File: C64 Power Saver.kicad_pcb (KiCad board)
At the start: 2 copper layers, 65.4 x 39.4 mm, 17 parts, among them J1 5V_INPUT, J2 5V_OUTPUT, J3 9VAC_INPUT, J4 9VAC_OUTPUT, K1 SANYOU_SRD_Form_C, Q1 PN2222A, Q2 PN2222A

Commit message: Oh... So I made a saver that works only on bad ones... Rev. B!
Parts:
- D1: value 4.7v -> 1N4732A
- D2: value 1N914 -> 1N4148
- D4: value OV -> BAD
- Q1, Q2: footprint TO_SOT_Packages_THT:TO-92_Molded_Narrow -> TO_SOT_Packages_THT:TO-92_Inline_Wide
- moved D4 8.71 mm to (125.2, 94.2)
- moved D3 7.83 mm to (125.2, 102.4)
- moved R4 3.81 mm to (109.2, 104.1)
- moved R5 3.81 mm to (109.2, 100.3)
- moved Q1 2.54 mm to (105.4, 102.9)
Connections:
- K1 pad 3: Net-(K1-Pad3) -> 5V_OUT
- K1 pad 4: 5V_OUT -> Net-(K1-Pad4)
- R5 pad 1: Net-(K1-Pad3) -> Net-(K1-Pad4)
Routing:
- net Net-(K1-Pad4): track 0.00 -> 21.9 mm
- net Net-(K1-Pad3): track 15.5 -> 0.00 mm
- net Net-(D3-Pad2): track 9.42 -> 4.04 mm
- net Net-(D1-Pad2): track 12.7 -> 15.8 mm
- net 5V_OUT: track 31.6 -> 28.6 mm
- net Net-(D4-Pad2): track 4.97 -> 7.46 mm
- net Net-(Q1-Pad3): track 31.2 -> 33.0 mm
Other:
- board text added: "C64 Power Saver Revision B https://hvetebolle.blogspot.com/"
- board text removed: "C64 Power Saver Revision A https://hvetebolle.blogspot.com/"

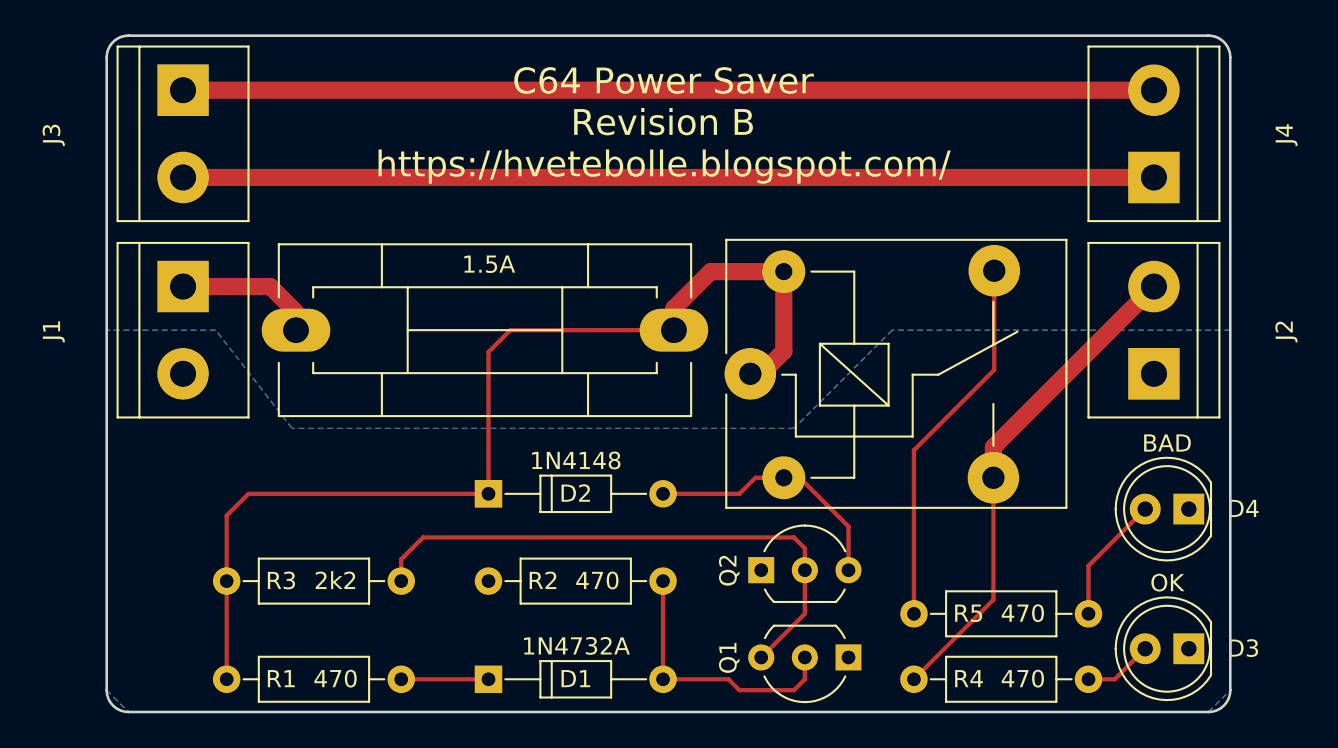
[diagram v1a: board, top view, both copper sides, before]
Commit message: PCB layout redone with DIN connector and added 5v buzzer
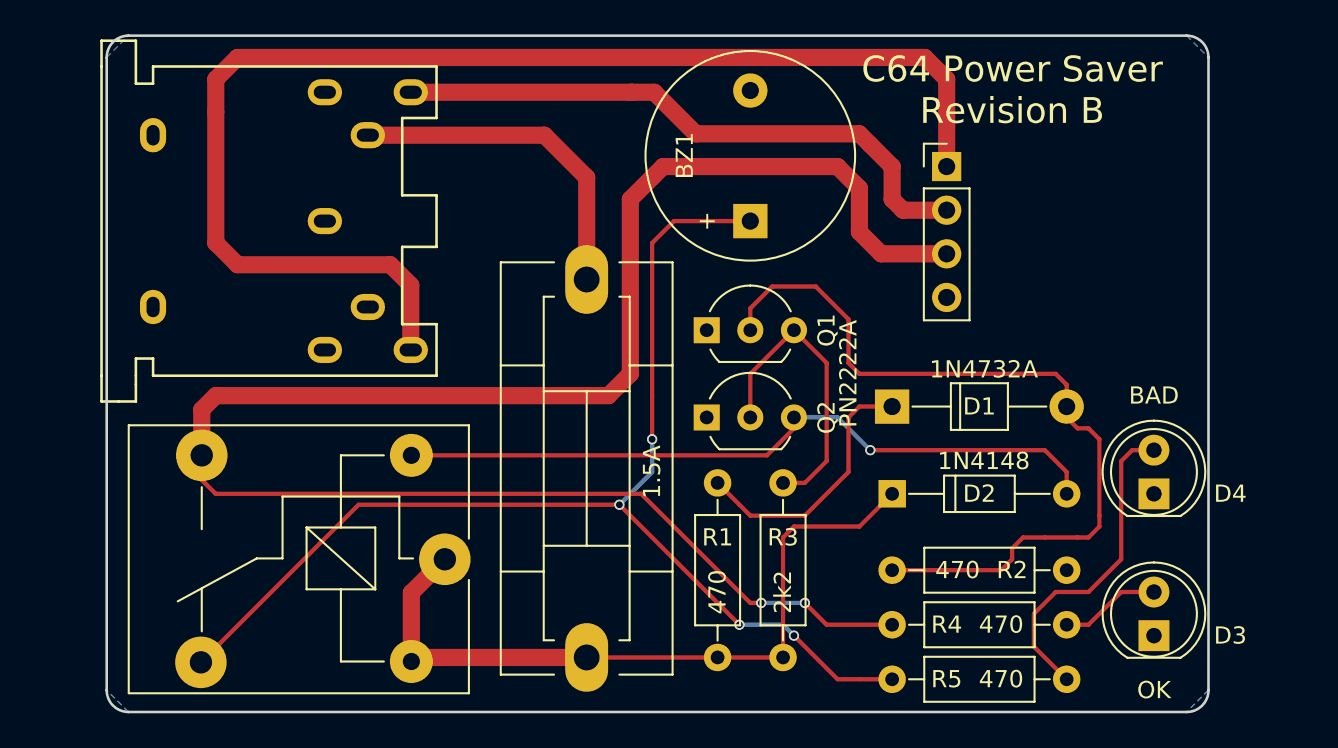
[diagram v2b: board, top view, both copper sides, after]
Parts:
- removed J2: 5V_OUTPUT, Connectors_Terminal_Blocks:TerminalBlock_bornier-2_P5.08mm
- removed J3: 9VAC_INPUT, Connectors_Terminal_Blocks:TerminalBlock_bornier-2_P5.08mm
- removed J4: 9VAC_OUTPUT, Connectors_Terminal_Blocks:TerminalBlock_bornier-2_P5.08mm
- added BZ1: Buzzer, Buzzers_Beepers:Buzzer_12x9.5RM7.6, F.Cu at (99.7, 77.5)
- added J5: DIN-7, C64_PWR:C64_PWR, F.Cu at (74.9, 77.5)
- D1: footprint Diodes_THT:D_DO-35_SOD27_P10.16mm_Horizontal -> Diodes_THT:D_T-1_P10.16mm_Horizontal
- J1: value 5V_INPUT -> OUTPUT; footprint Connectors_Terminal_Blocks:TerminalBlock_bornier-2_P5.08mm -> C64_PWR:OUTPUT_ZIP
- moved J1 45.0 mm to (111.1, 74.3), turned to 0 degrees
- moved R3 32.7 mm to (101.6, 102.9), turned to 90 degrees
- moved R1 28.6 mm to (97.8, 102.9), turned to 90 degrees
- moved D1 28.4 mm to (108.0, 88.3)
- moved D2 23.5 mm to (108.0, 93.3)
- moved K1 20.8 mm to (81.9, 97.2), turned to 180 degrees
- moved Q1 20.8 mm to (97.2, 83.8), turned to 0 degrees
- moved F1 19.7 mm to (90.2, 102.9), turned to 90 degrees
- moved R2 13.4 mm to (108.0, 97.8), turned to 0 degrees
- moved Q2 9.44 mm to (97.2, 88.9)
- moved R5 4.02 mm to (108.0, 104.1)
- moved R4 3.42 mm to (108.0, 101.0)
- moved D4 2.22 mm to (123.2, 93.3), turned to 90 degrees
- moved D3 2.17 mm to (123.2, 101.6), turned to 90 degrees
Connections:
- J1 pad 1: 5V_IN -> 9VAC_2
- J1 pad 2: GND -> 9VAC_1
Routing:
- net 5V_OUT: track 28.6 -> 106.5 mm, vias 0 -> 2
- net Net-(BZ1-Pad1): track 21.9 -> 70.5 mm, vias 0 -> 4
- net Net-(D1-Pad2): track 15.8 -> 47.0 mm
- net Net-(D2-Pad2): track 14.9 -> 42.0 mm, vias 0 -> 1
- net 9VAC_1: track 56.5 -> 35.2 mm
- net 9VAC_2: track 56.5 -> 74.5 mm
- net Net-(D2-Pad1): track 60.5 -> 42.9 mm
- net Net-(Q1-Pad3): track 33.0 -> 17.6 mm
- net 5V_IN: track 8.24 -> 19.7 mm
- net Net-(D4-Pad2): track 7.46 -> 18.9 mm
- net Net-(D1-Pad1): track 5.08 -> 15.4 mm
- net Net-(D3-Pad2): track 4.04 -> 5.87 mm
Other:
- board size 65.4 x 39.4 mm -> 64.1 x 39.4 mm
- board text added: "C64 Power Saver Revision B"
- board text added: "https://hvetebolle.blogspot.com/"
- board text removed: "5V INPUT"
- board text removed: "5V OUTPUT"
- board text removed: "9V AC"
- board text removed: "C64 Power Saver Revision B https://hvetebolle.blogspot.com/"
- board text removed: "GND"

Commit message: Fixed groundplane and made wire solder points larger
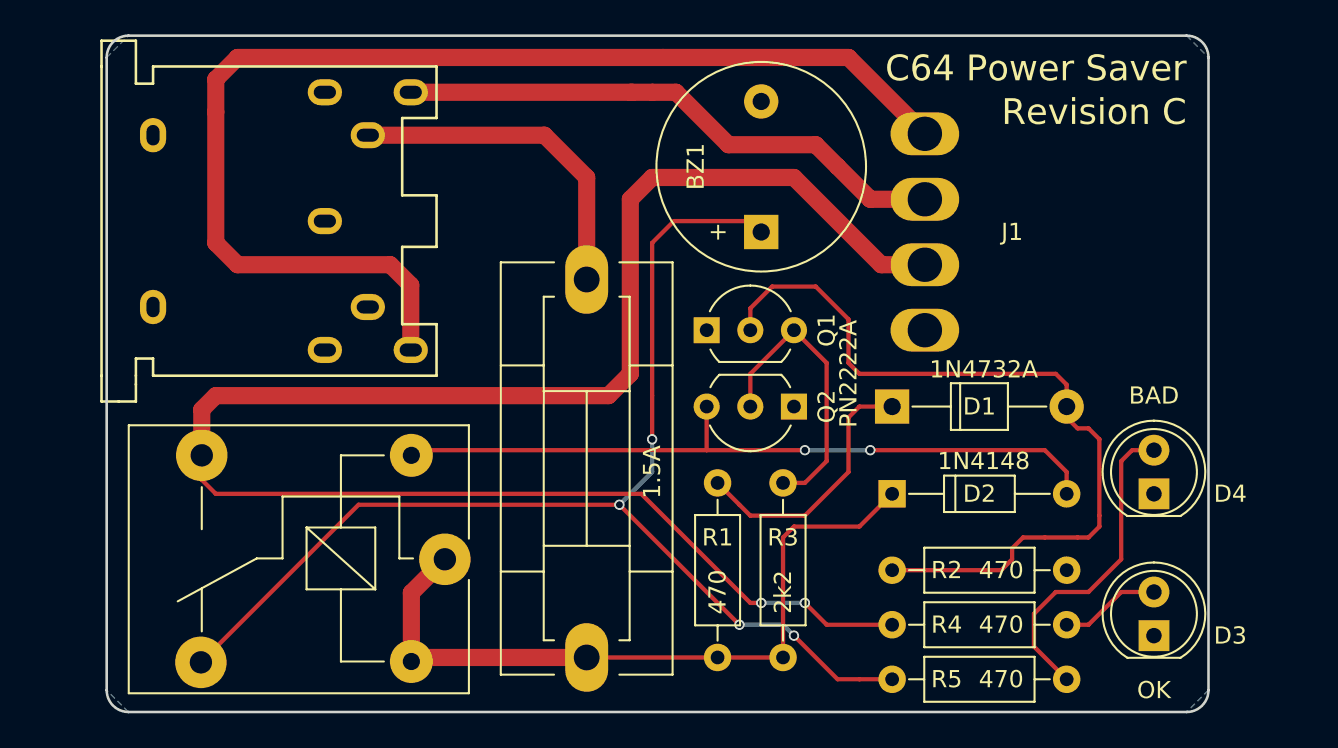
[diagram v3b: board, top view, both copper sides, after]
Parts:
- moved Q2 5.12 mm to (102.2, 88.3), turned to 180 degrees
- moved BZ1 0.90 mm to (100.3, 78.1)
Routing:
- net 9VAC_2: track 74.5 -> 69.4 mm
- net 5V_OUT: track 106.5 -> 103.5 mm
- net 9VAC_1: track 35.2 -> 32.5 mm
- net Net-(Q1-Pad3): track 17.6 -> 17.0 mm
- net Net-(D2-Pad2): track 42.0 -> 42.6 mm, vias 1 -> 2
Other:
- board text added: "C64 Power Saver"
- board text added: "Revision C"
- board text removed: "C64 Power Saver Revision B"

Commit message: Added wire pads for +5v and GND for thicker wires when internal mounting
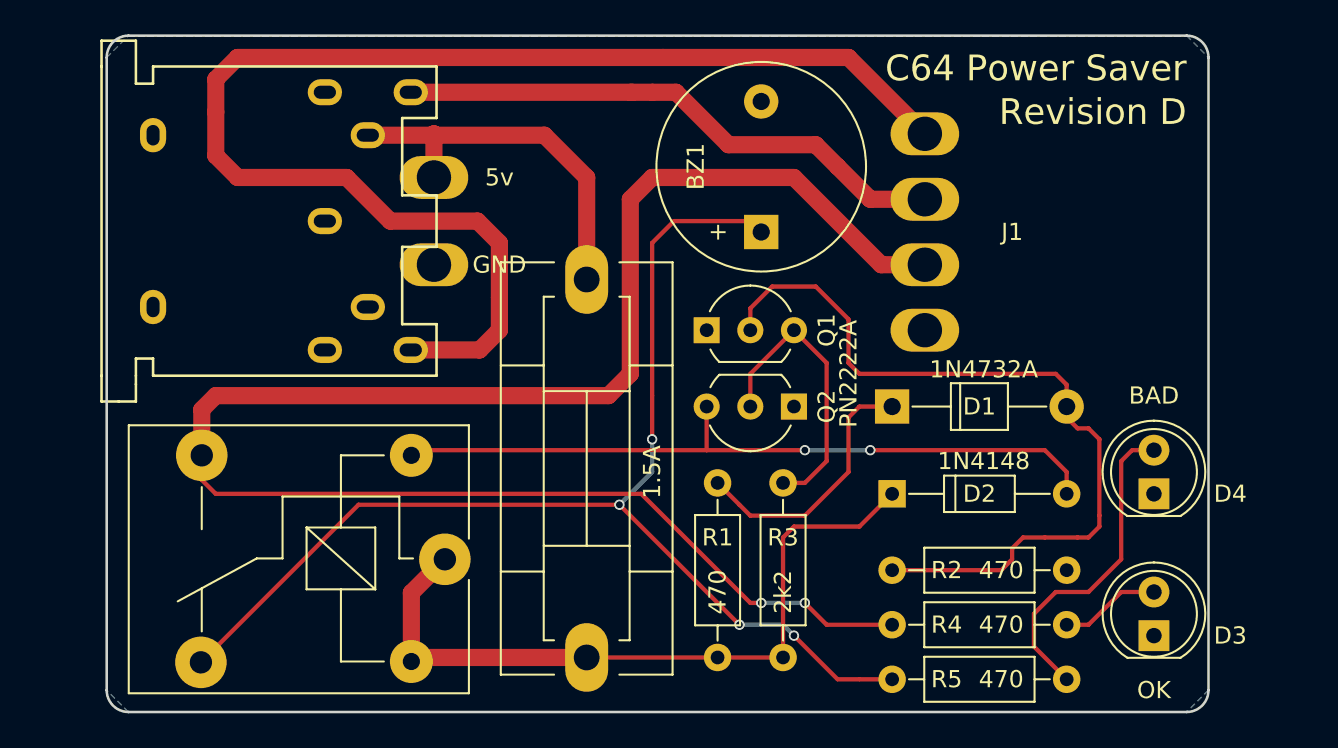
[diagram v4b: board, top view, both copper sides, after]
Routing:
- net 9VAC_2: track 69.4 -> 77.4 mm
- net 5V_IN: track 19.7 -> 22.3 mm
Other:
- board text added: "Revision D"
- board text removed: "Revision C"

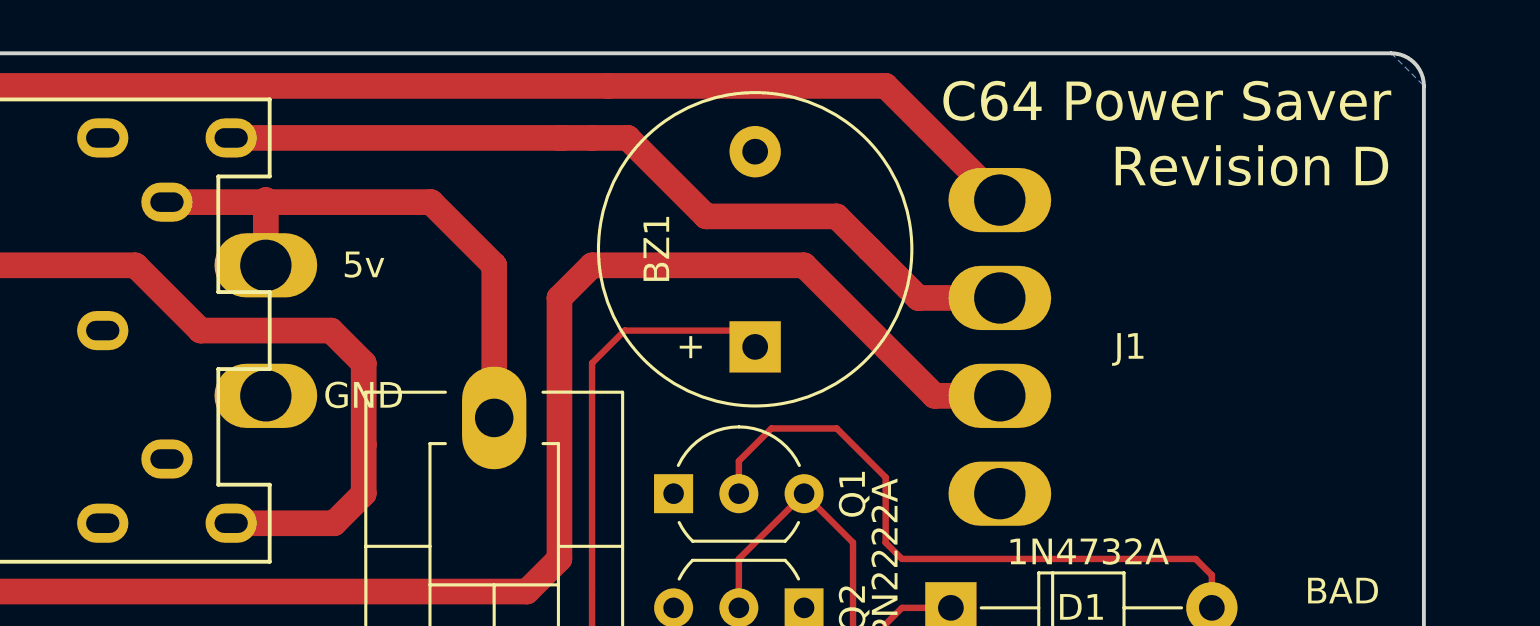
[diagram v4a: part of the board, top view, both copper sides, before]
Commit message: Add 5v to DIN-7 pin 4
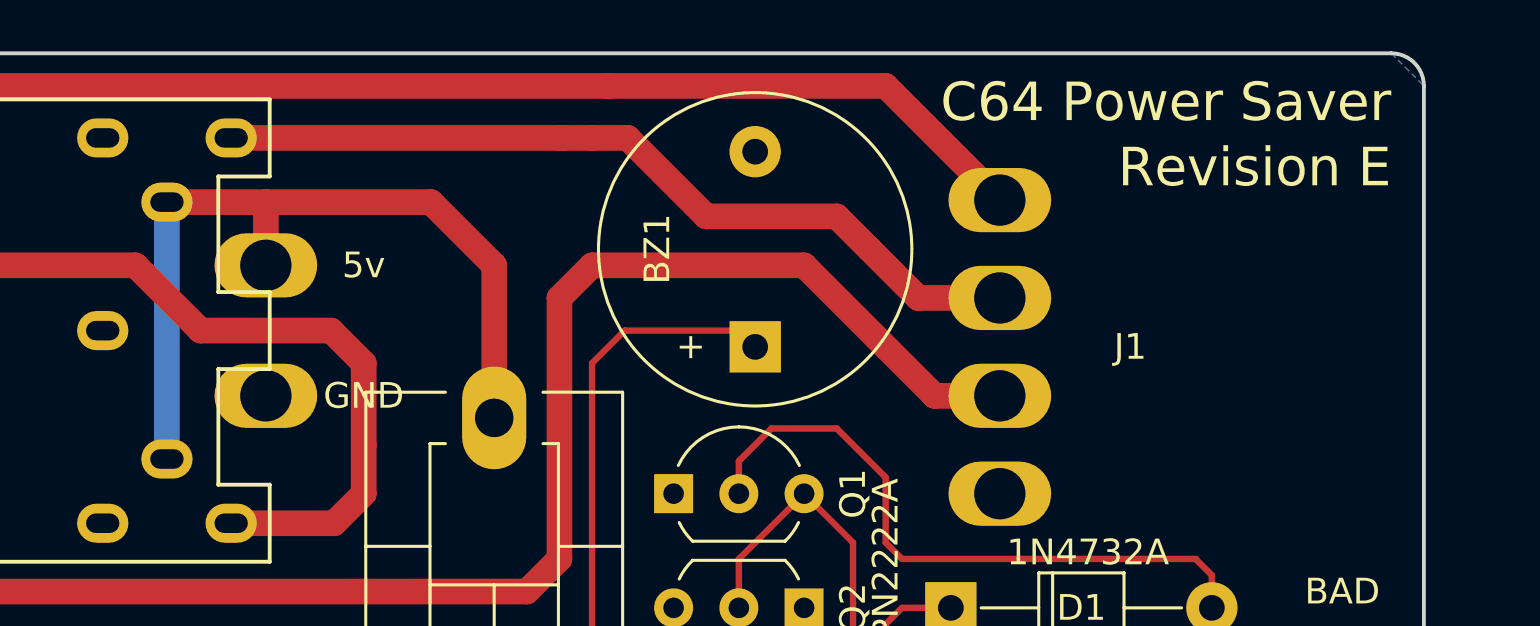
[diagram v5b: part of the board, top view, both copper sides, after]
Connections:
- J5 pad 4: (no net) -> 5V_IN
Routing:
- net 5V_IN: track 22.3 -> 32.2 mm
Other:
- board text added: "Revision E"
- board text added: "github.com/tebl"
- board text removed: "Revision D"
- board text removed: "https://hvetebolle.blogspot.com/"
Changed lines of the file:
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@@
 (kicad_pcb (version 4) (host pcbnew 4.0.7)
   (general
-    (links 30)
+    (links 31)
     (no_connects 0)
     (area 62.154999 66.599999 126.440001 106.120001)
     (thickness 1.6)
     (drawings 11)
-    (tracks 136)
+    (tracks 135)
     (zones 0)
     (modules 16)
@@
     (pad 5 thru_hole oval (at -5 -2.5 270) (size 1.524 2) (drill oval 0.762 1.3) (layers *.Cu *.Mask)
       (net 9 5V_IN))
-    (pad 4 thru_hole oval (at 5 -2.5 270) (size 1.524 2) (drill oval 0.762 1.3) (layers *.Cu *.Mask))
+    (pad 4 thru_hole oval (at 5 -2.5 270) (size 1.524 2) (drill oval 0.762 1.3) (layers *.Cu *.Mask)
+      (net 9 5V_IN))
     (pad 3 thru_hole oval (at -7.5 0 270) (size 1.524 2) (drill oval 0.762 1.3) (layers *.Cu *.Mask))
     (pad 1 thru_hole oval (at 7.5 0 270) (size 1.524 2) (drill oval 0.762 1.3) (layers *.Cu *.Mask))
@@
       (net 12 9VAC_1))
   )
-  (gr_text "Revision D" (at 125.095 71.12) (layer F.SilkS)
+  (gr_text "Revision E" (at 125.095 71.12) (layer F.SilkS)
     (effects (font (size 1.5 1.5) (thickness 0.3)) (justify right))
   )
-  (gr_text https://hvetebolle.blogspot.com/ (at 123.825 67.945) (layer B.SilkS)
+  (gr_text github.com/tebl (at 123.825 67.945) (layer B.SilkS)
     (effects (font (size 1.5 1.5) (thickness 0.3)) (justify left mirror))
   )
@@
   (segment (start 104.14 91.44) (end 104.14 85.725) (width 0.25) (layer F.Cu) (net 8))
   (segment (start 104.14 85.725) (end 102.235 83.82) (width 0.25) (layer F.Cu) (net 8))
-  (segment (start 81.28 74.93) (end 81.28 72.47) (width 1) (layer F.Cu) (net 9))
-  (segment (start 81.28 72.47) (end 81.28 72.39) (width 1) (layer F.Cu) (net 9))
-  (segment (start 81.28 72.39) (end 81.28 72.47) (width 1) (layer F.Cu) (net 9))
+  (segment (start 81.28 72.47) (end 81.28 74.93) (width 1) (layer F.Cu) (net 9))
+  (segment (start 77.43 82.47) (end 77.43 72.47) (width 1) (layer B.Cu) (net 9))
   (segment (start 77.43 72.47) (end 81.28 72.47) (width 1) (layer F.Cu) (net 9))
   (segment (start 81.28 72.47) (end 87.71 72.47) (width 1) (layer F.Cu) (net 9))
@@
   (segment (start 92.71 76.2) (end 92.71 86.36) (width 1) (layer F.Cu) (net 10))
   (segment (start 67.765 91.105) (end 67.765 92.53) (width 0.25) (layer F.Cu) (net 10))
-  (segment (start 79.93 84.97) (end 83.94 84.97) (width 1) (layer F.Cu) (net 11) (status 400000))
+  (segment (start 79.93 84.97) (end 83.94 84.97) (width 1) (layer F.Cu) (net 11))
   (segment (start 105.41 67.945) (end 109.855 72.39) (width 1) (layer F.Cu) (net 11))
   (segment (start 69.85 67.945) (end 94.615 67.945) (width 1) (layer F.Cu) (net 11))
